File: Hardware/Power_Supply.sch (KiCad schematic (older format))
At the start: 5 parts

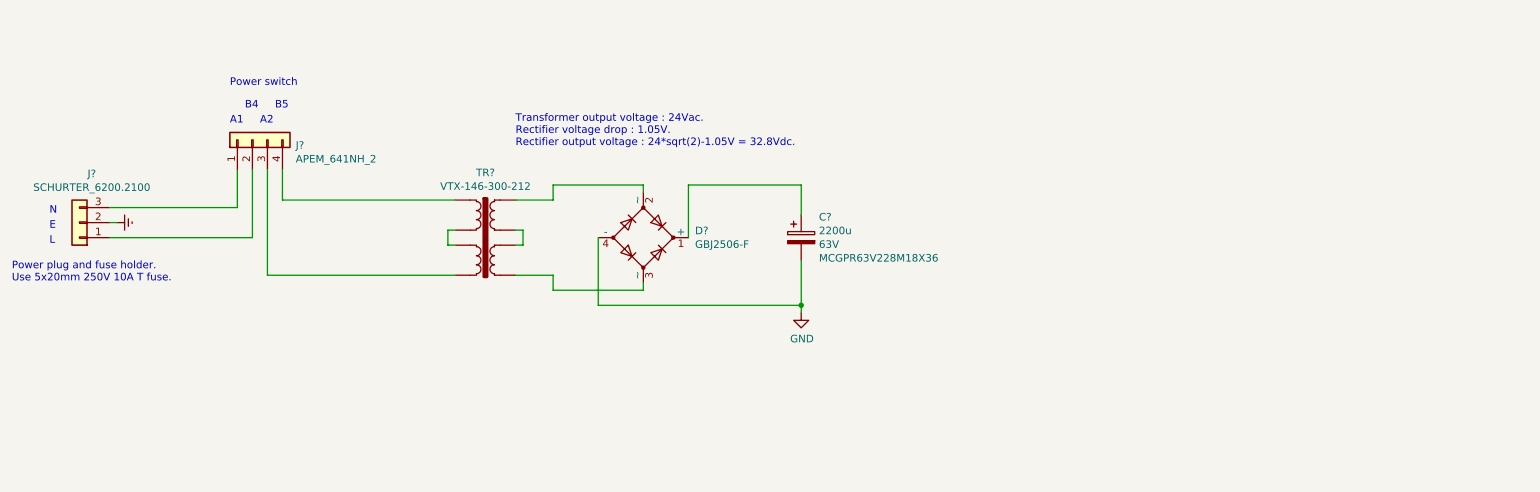
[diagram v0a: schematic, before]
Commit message: [Hardware] Added power supply regulator schematic.
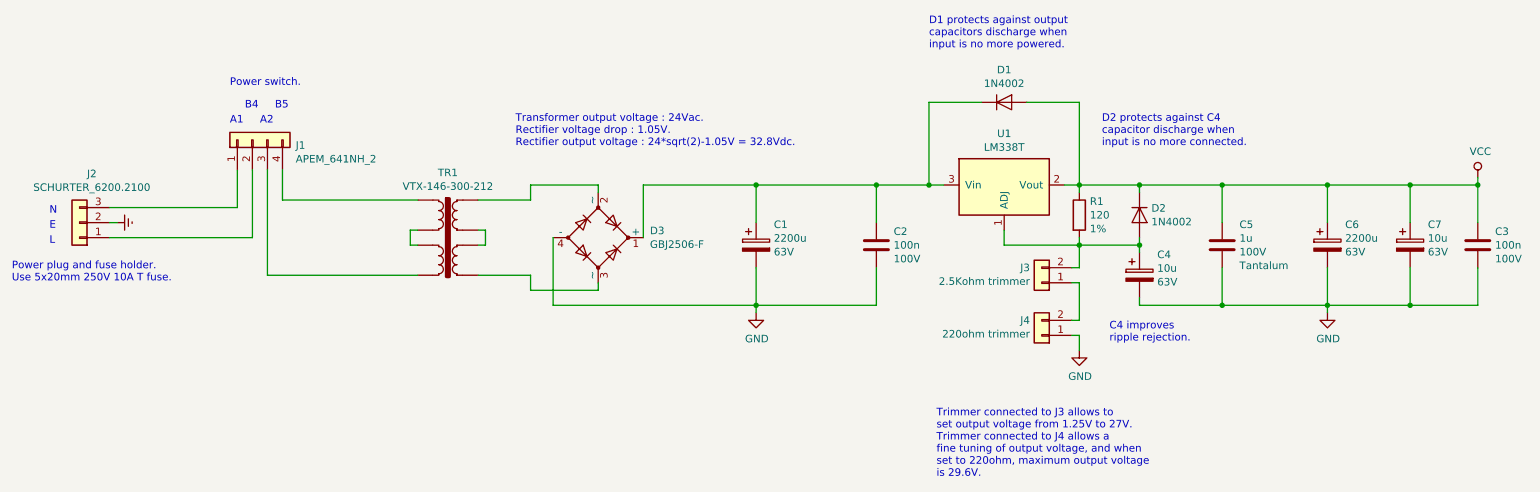
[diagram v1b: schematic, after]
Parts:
- added C2, C3: 100n, symbol Device:C
- added C4, C7: 10u, symbol Device:CP
- added C5: 1u, symbol Device:C
- added C6: 2200u, symbol Device:CP
- added D1, D2: 1N4002, Diode_THT:D_DO-41_SOD81_P10.16mm_Horizontal, symbol Diode:1N4002
- added J3: 2.5Kohm trimmer, symbol Connector_Generic:Conn_01x02
- added J4: 220ohm trimmer, symbol Connector_Generic:Conn_01x02
- added R1: 120, symbol Device:R
- added U1: LM338T, Package_TO_SOT_THT:TO-220-3_Vertical, symbol LM338T:LM338T
- gave numbers to parts that had none: 5
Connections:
- net GND: now also C2.2, C3.2, C4.2, C5.2, C6.2, C7.2, J4.1 (Pin_1)
- net at C1.1, D3.1 (+): now also C2.1, D1.1 (K), U1.3 (Vin)
- new net: C4.1, D2.2 (A), J3.2 (Pin_2), R1.2, U1.1 (ADJ)
- new net: J3.1 (Pin_1), J4.2 (Pin_2)
- new net VCC: C3.1, C5.1, C6.1, C7.1, D1.2 (A), D2.1 (K), R1.1, U1.2 (Vout)
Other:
- note added: "C4 improves\nripple rejection."
- note added: "D1 protects against output\ncapacitors discharge when\ninput is no more powered."
- note added: "D2 protects against C4\ncapacitor discharge when\ninput is no more connected."
- note added: "Power switch."
- note added: "Trimmer connected to J3 allows to\nset output voltage from 1.25V to 27V.\nTrimmer connected to J4 allows a\nfine tuning of output voltage, and when\nset to 220ohm, maximum output voltage\nis 29.6V."
- note removed: "Power switch"
- moved on the sheet: C1, D3, TR1
